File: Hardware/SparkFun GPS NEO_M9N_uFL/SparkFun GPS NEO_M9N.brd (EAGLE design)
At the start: 40.6 x 33 mm, 93 parts, among them J13 U.FL, J2 Qwiic Right Angle, J4 Qwiic Right Angle, U1 U-BLOX_NEO-M9N, U2 3.3V

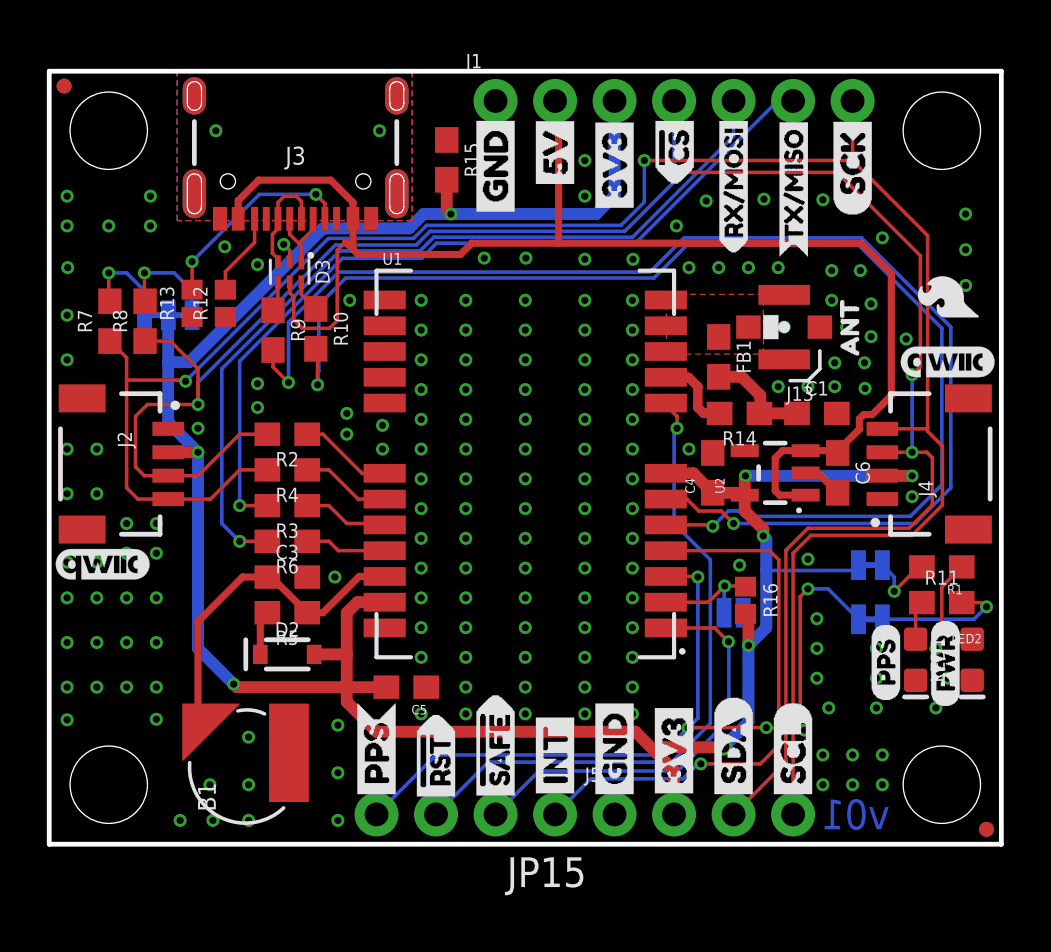
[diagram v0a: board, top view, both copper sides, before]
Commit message: Fixes small DRC problems, Adds silk to battery, adds production id to NEO-M9N chip
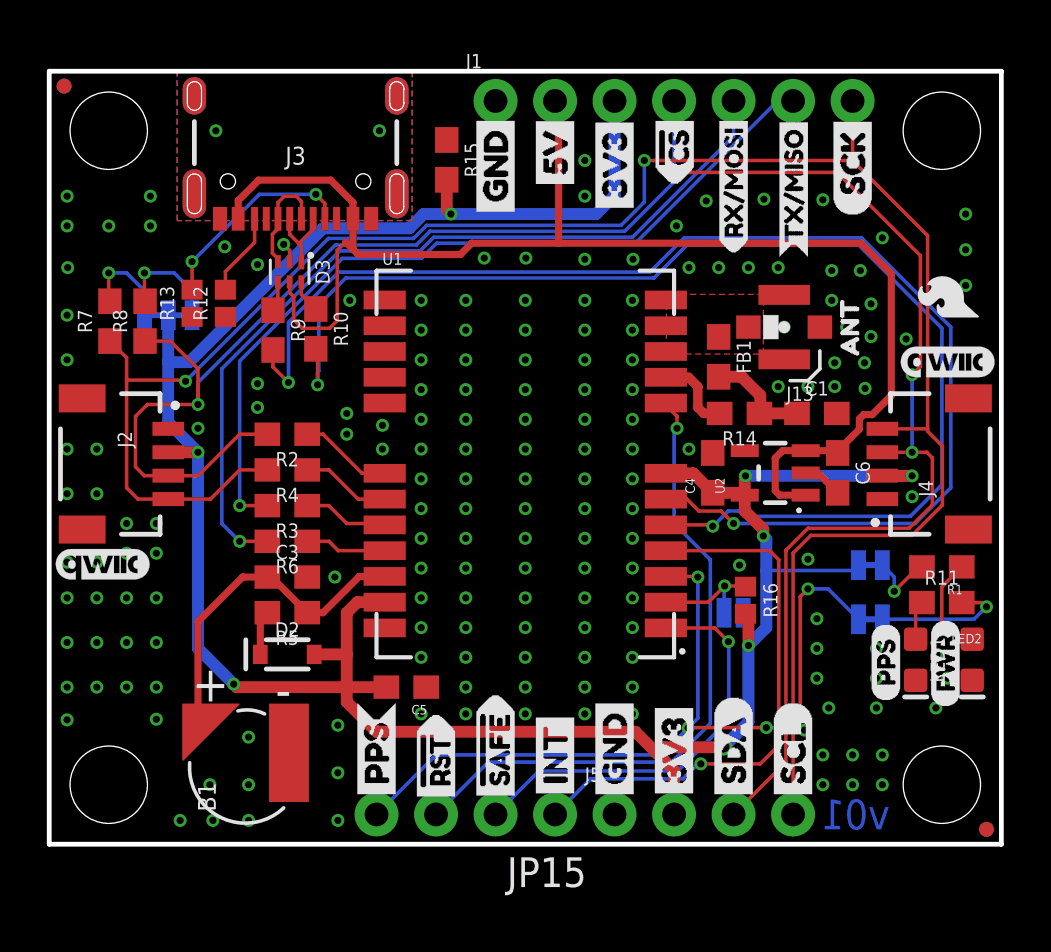
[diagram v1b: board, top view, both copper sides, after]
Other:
- board text added: "+"
- board text added: "-"
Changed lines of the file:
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@@
 <drawing>
 <settings>
-<setting alwaysvectorfont="yes"/>
+<setting alwaysvectorfont="no"/>
 <setting keepoldvectorfont="yes"/>
 <setting verticaltext="up"/>
 </settings>
-<grid distance="0.01" unitdist="inch" unit="inch" style="lines" multiple="1" display="yes" altdistance="0.005" altunitdist="inch" altunit="inch"/>
+<grid distance="0.01" unitdist="inch" unit="inch" style="lines" multiple="1" display="yes" altdistance="0.001" altunitdist="inch" altunit="inch"/>
 <layers>
 <layer number="1" name="Top" color="4" fill="1" visible="yes" active="yes"/>
@@
 <layer number="37" name="tTest" color="7" fill="1" visible="no" active="yes"/>
 <layer number="38" name="bTest" color="7" fill="1" visible="no" active="yes"/>
-<layer number="39" name="tKeepout" color="4" fill="11" visible="yes" active="yes"/>
+<layer number="39" name="tKeepout" color="4" fill="11" visible="no" active="yes"/>
 <layer number="40" name="bKeepout" color="1" fill="11" visible="no" active="yes"/>
 <layer number="41" name="tRestrict" color="4" fill="10" visible="no" active="yes"/>
@@
 <layer number="115" name="ReferenceISLANDS" color="7" fill="1" visible="no" active="no"/>
 <layer number="116" name="Patch_BOT" color="9" fill="4" visible="no" active="no"/>
-<layer number="117" name="PM_Ref" color="26" fill="1" visible="no" active="yes"/>
+<layer number="117" name="PM_Ref" color="26" fill="1" visible="yes" active="yes"/>
 <layer number="118" name="Rect_Pads" color="7" fill="1" visible="no" active="no"/>
-<layer number="119" name="PF_Ref" color="31" fill="1" visible="no" active="yes"/>
-<layer number="120" name="WFL_Ref" color="25" fill="1" visible="no" active="yes"/>
+<layer number="119" name="PF_Ref" color="31" fill="1" visible="yes" active="yes"/>
+<layer number="120" name="WFL_Ref" color="25" fill="1" visible="yes" active="yes"/>
 <layer number="121" name="_tsilk" color="7" fill="1" visible="no" active="no"/>
 <layer number="122" name="_bsilk" color="7" fill="1" visible="no" active="no"/>
@@
 <dimension x1="2.54" y1="30.48" x2="38.1" y2="30.48" x3="20.32" y3="45.72" textsize="1.778" textratio="15" layer="47" unit="inch"/>
 <text x="12.7" y="-17.78" size="1.778" layer="51" font="vector">Elias Santistevan</text>
+<text x="9.652" y="5.842" size="1.524" layer="21" font="vector" ratio="15">-</text>
+<text x="6.096" y="6.096" size="1.524" layer="21" font="vector" ratio="15">+</text>
 </plain>
 <attributes>
@@
 <element name="U1" library="gps" package="NEO-M9N" value="U-BLOX_NEO-M9N" x="20.32" y="16.2306" smashed="yes">
 <attribute name="NAME" x="14.22" y="24.7306" size="0.508" layer="25"/>
+<attribute name="PROD_ID" value="IC-14651" x="20.32" y="16.2306" size="1.778" layer="27" display="off"/>
 <attribute name="VALUE" x="14.22" y="7.2306" size="0.508" layer="27"/>
 </element>
@@
 <via x="35.56" y="2.54" extent="1-16" drill="0.3048"/>
 <via x="35.56" y="3.81" extent="1-16" drill="0.3048"/>
-<via x="37.846" y="8.3566" extent="1-16" drill="0.3048"/>
+<via x="37.8968" y="8.1026" extent="1-16" drill="0.3048"/>
 <via x="6.858" y="2.54" extent="1-16" drill="0.3048"/>
 <via x="5.588" y="1.016" extent="1-16" drill="0.3048"/>
@@
 <contactref element="LED1" pad="A"/>
 <contactref element="R11" pad="1"/>
-<wire x1="36.9824" y1="8.751" x2="36.7794" y2="8.751" width="0.1524" layer="1"/>
 <wire x1="36.9824" y1="8.751" x2="36.9824" y2="10.0448" width="0.1524" layer="1"/>
 <wire x1="36.9824" y1="10.0448" x2="37.25" y2="10.3124" width="0.1524" layer="1"/>
